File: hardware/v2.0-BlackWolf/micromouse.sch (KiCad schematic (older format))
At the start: 50 parts, among them CN1 7_PIN_HEADER, CN2 5_PIN_HEADER, M3 2.54MM-SLIDE-SWITCH_TS02_SWIT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, P1 B3B-PH-SM4-TB, P2 B3B-PH-SM4-TB, SW1 SWITCH_DPST, SW2 SWITCH_DPST, SW3 SWITCH_DPST, U1 STM32F446RE_LQFP64, U11 TPS76850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

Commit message: PCB: Fixed UART pins
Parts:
- CN1: value 7_PIN_HEADER -> 6_PIN_HEADER; footprint Pin_Headers:Pin_Header_Straight_1x07_Pitch2.54mm -> Pin_Headers:Pin_Header_Straight_1x06_Pitch2.54mm; symbol 7_PIN_HEADER -> 6_PIN_HEADER
- CN2: value 5_PIN_HEADER -> 6_PIN_HEADER
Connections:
- net +3V3: no longer CN1.7
- net +5V: now also CN1.4
- net GND: now also CN1.6; no longer CN1.1
- net USART_RX: now also CN1.2; no longer CN1.4
- net USART_TX: now also CN1.3; no longer CN1.5
- no-connect marks 25 -> 24

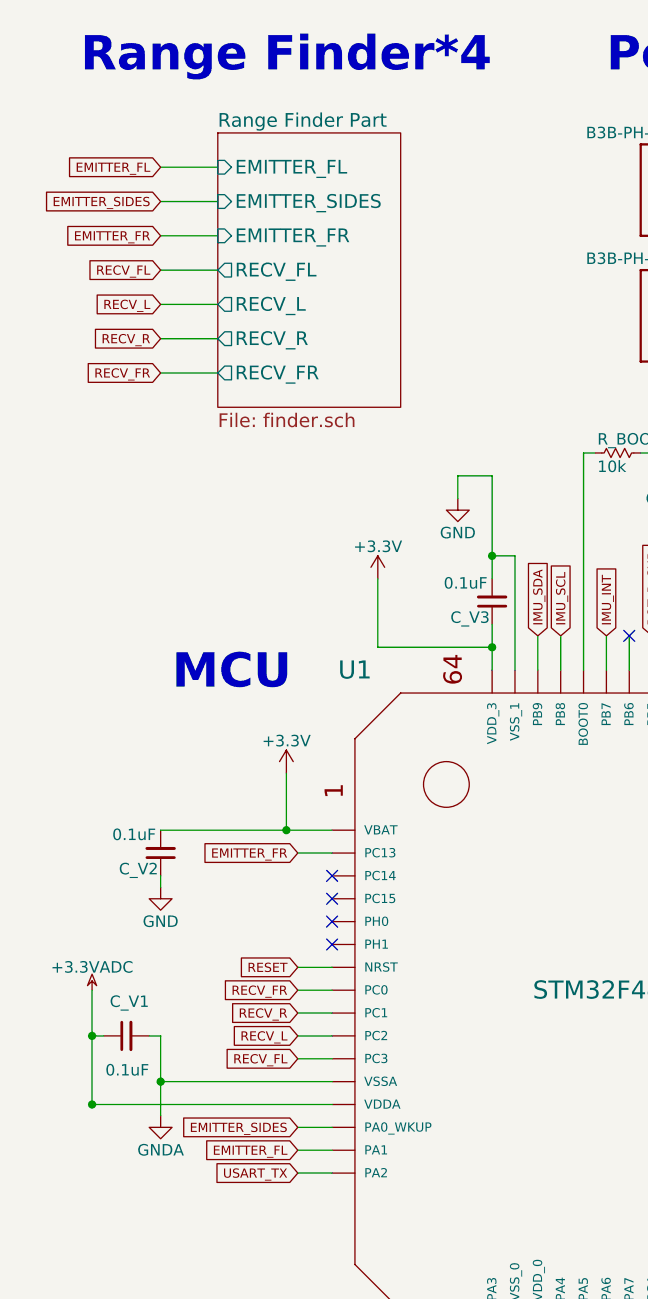
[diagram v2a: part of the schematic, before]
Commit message: PCB: Added IR LED switch line
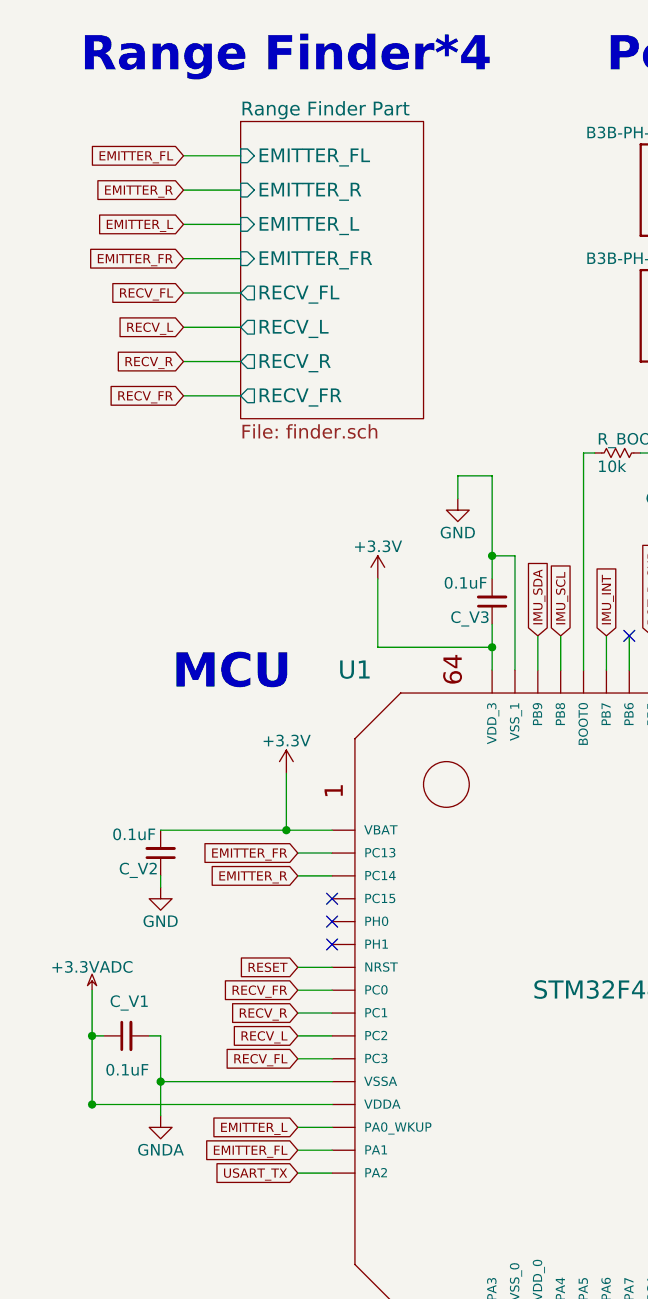
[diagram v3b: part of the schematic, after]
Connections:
- net EMITTER_R: now reaches U1.PC14
- net EMITTER_SIDES renamed EMITTER_L
- no-connect marks 24 -> 23
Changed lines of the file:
@@
 $EndSheet
 $Sheet
-S 1350 1200 800  1200
+S 1450 1150 800  1300
 U 56EB6D2D
 F0 "Range Finder Part" 60
 F1 "finder.sch" 60
-F2 "EMITTER_FL" I L 1350 1350 60
-F3 "EMITTER_SIDES" I L 1350 1500 60
-F4 "EMITTER_FR" I L 1350 1650 60
-F5 "RECV_FL" O L 1350 1800 60
-F6 "RECV_L" O L 1350 1950 60
-F7 "RECV_R" O L 1350 2100 60
-F8 "RECV_FR" O L 1350 2250 60
+F2 "EMITTER_FL" I L 1450 1300 60
+F3 "EMITTER_FR" I L 1450 1750 60
+F4 "RECV_FL" O L 1450 1900 60
+F5 "RECV_L" O L 1450 2050 60
+F6 "RECV_R" O L 1450 2200 60
+F7 "RECV_FR" O L 1450 2350 60
+F8 "EMITTER_L" I L 1450 1600 60
+F9 "EMITTER_R" I L 1450 1450 60
 $EndSheet
 $Sheet
@@
 Text GLabel 1700 4350 0    40   Input ~ 0
 EMITTER_FR
-Text GLabel 1100 1650 0    40   Input ~ 0
+Text GLabel 1200 1750 0    40   Input ~ 0
 EMITTER_FR
 Text GLabel 1700 5550 0    40   Input ~ 0
-EMITTER_SIDES
+EMITTER_L
 Text GLabel 1700 5650 0    40   Input ~ 0
 EMITTER_FL
-Text GLabel 1100 1500 0    40   Input ~ 0
-EMITTER_SIDES
-Text GLabel 1100 1350 0    40   Input ~ 0
+Text GLabel 1200 1600 0    40   Input ~ 0
+EMITTER_L
+Text GLabel 1200 1300 0    40   Input ~ 0
 EMITTER_FL
 Text GLabel 1700 4950 0    40   Input ~ 0
@@
 Text GLabel 1700 5250 0    40   Input ~ 0
 RECV_FL
-Text GLabel 1100 2250 0    40   Input ~ 0
+Text GLabel 1200 2350 0    40   Input ~ 0
 RECV_FR
-Text GLabel 1100 2100 0    40   Input ~ 0
+Text GLabel 1200 2200 0    40   Input ~ 0
 RECV_R
-Text GLabel 1100 1950 0    40   Input ~ 0
+Text GLabel 1200 2050 0    40   Input ~ 0
 RECV_L
-Text GLabel 1100 1800 0    40   Input ~ 0
+Text GLabel 1200 1900 0    40   Input ~ 0
 RECV_FL
-NoConn ~ 1850 4450
 NoConn ~ 1850 4550
 NoConn ~ 1850 4650
@@
 	3350 3400 3350 3550
 Wire Wire Line
-	1350 2250 1100 2250
-Wire Wire Line
-	1100 2100 1350 2100
-Wire Wire Line
-	1350 1950 1100 1950
-Wire Wire Line
-	1100 1800 1350 1800
-Wire Wire Line
-	1100 1650 1350 1650
-Wire Wire Line
-	1100 1500 1350 1500
-Wire Wire Line
-	1100 1350 1350 1350
+	1450 2350 1200 2350
+Wire Wire Line
+	1200 2200 1450 2200
+Wire Wire Line
+	1450 2050 1200 2050
+Wire Wire Line
+	1200 1900 1450 1900
+Wire Wire Line
+	1200 1750 1450 1750
+Wire Wire Line
+	1200 1600 1450 1600
+Wire Wire Line
+	1200 1300 1450 1300
 Wire Wire Line
 	3050 6600 3050 6450
@@
 	1    0    0    -1
 $EndComp
+Text GLabel 1200 1450 0    40   Input ~ 0
+EMITTER_R
+Wire Wire Line
+	1200 1450 1450 1450
+Text GLabel 1700 4450 0    40   Input ~ 0
+EMITTER_R
+Wire Wire Line
+	1700 4450 1850 4450
 $EndSCHEMATC
